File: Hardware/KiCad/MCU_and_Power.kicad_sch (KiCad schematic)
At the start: 67 parts

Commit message: Final schematic changes made, added some annotations
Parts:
- HSE?: footprint (none) -> Crystal:Crystal_SMD_3225-4Pin_3.2x2.5mm
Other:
- note added: "ADC1_INP3"
- note added: "Pins with possible external connections have current limiting resistors"
- note added: "TIM3_CH4"
- note added: "TIM4_CH1"
- note added: "TIM4_CH2"
- note added: "TIM4_CH3"
- note added: "TIM4_CH4"
- note added: "TIM5_CH3"
- note added: "TIM5_CH4"
- note removed: "Pins with external connection have current limiting resistors"
- note removed: "check"

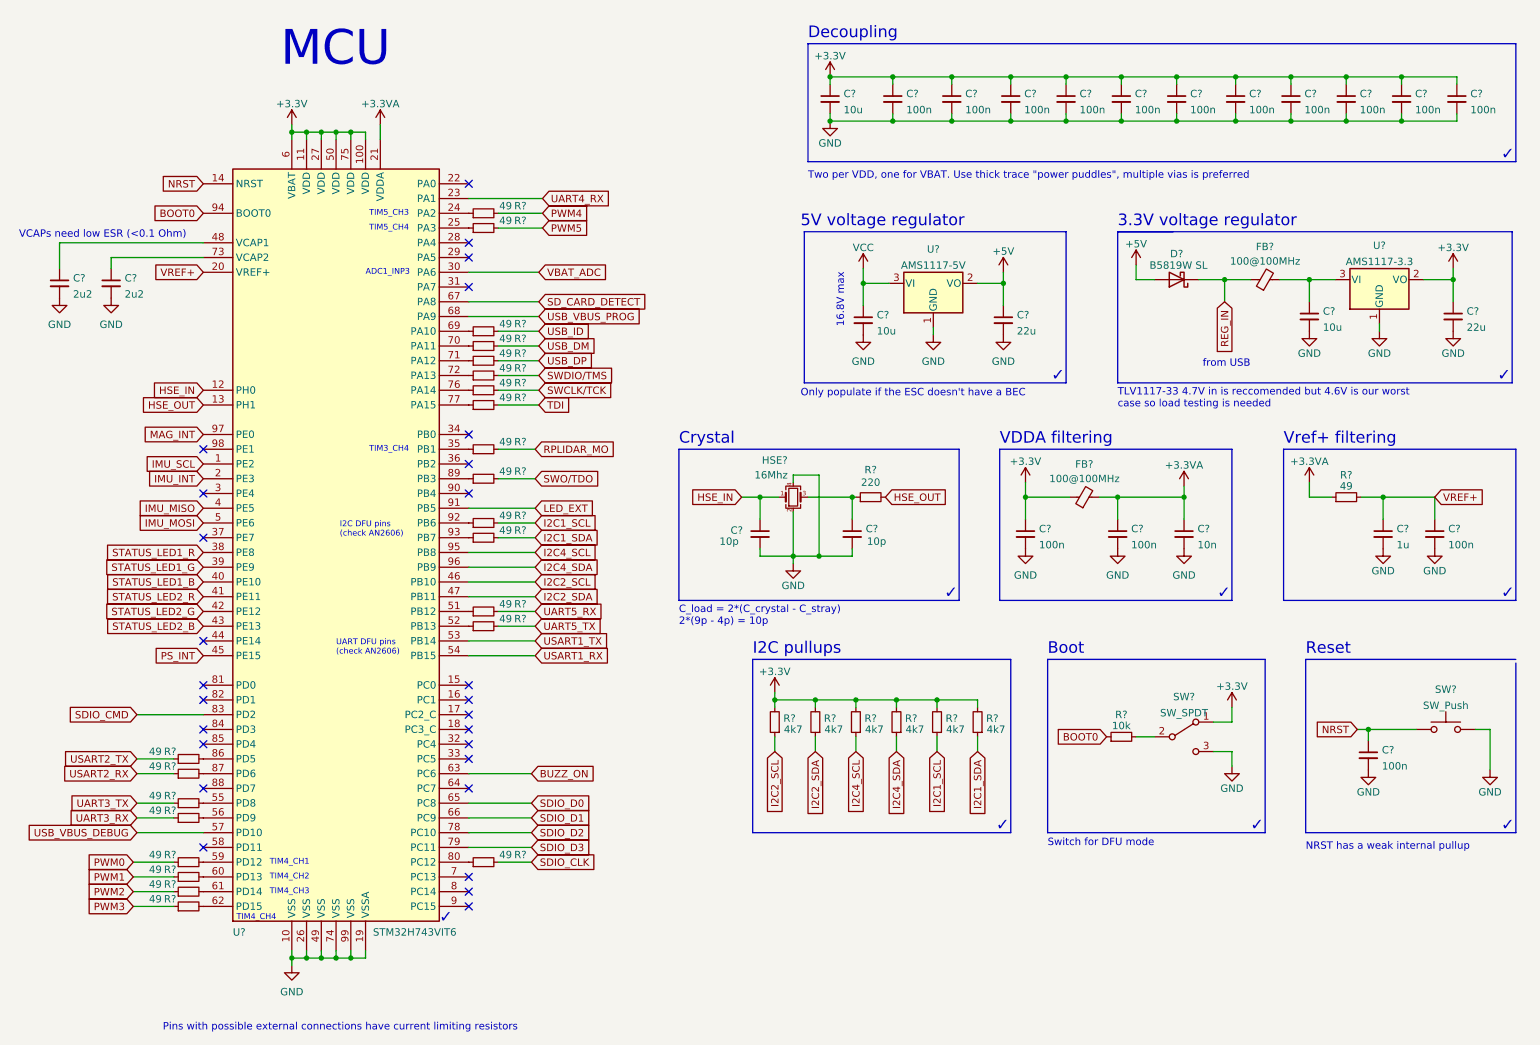
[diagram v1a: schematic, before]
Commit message: Fixed ERC errors
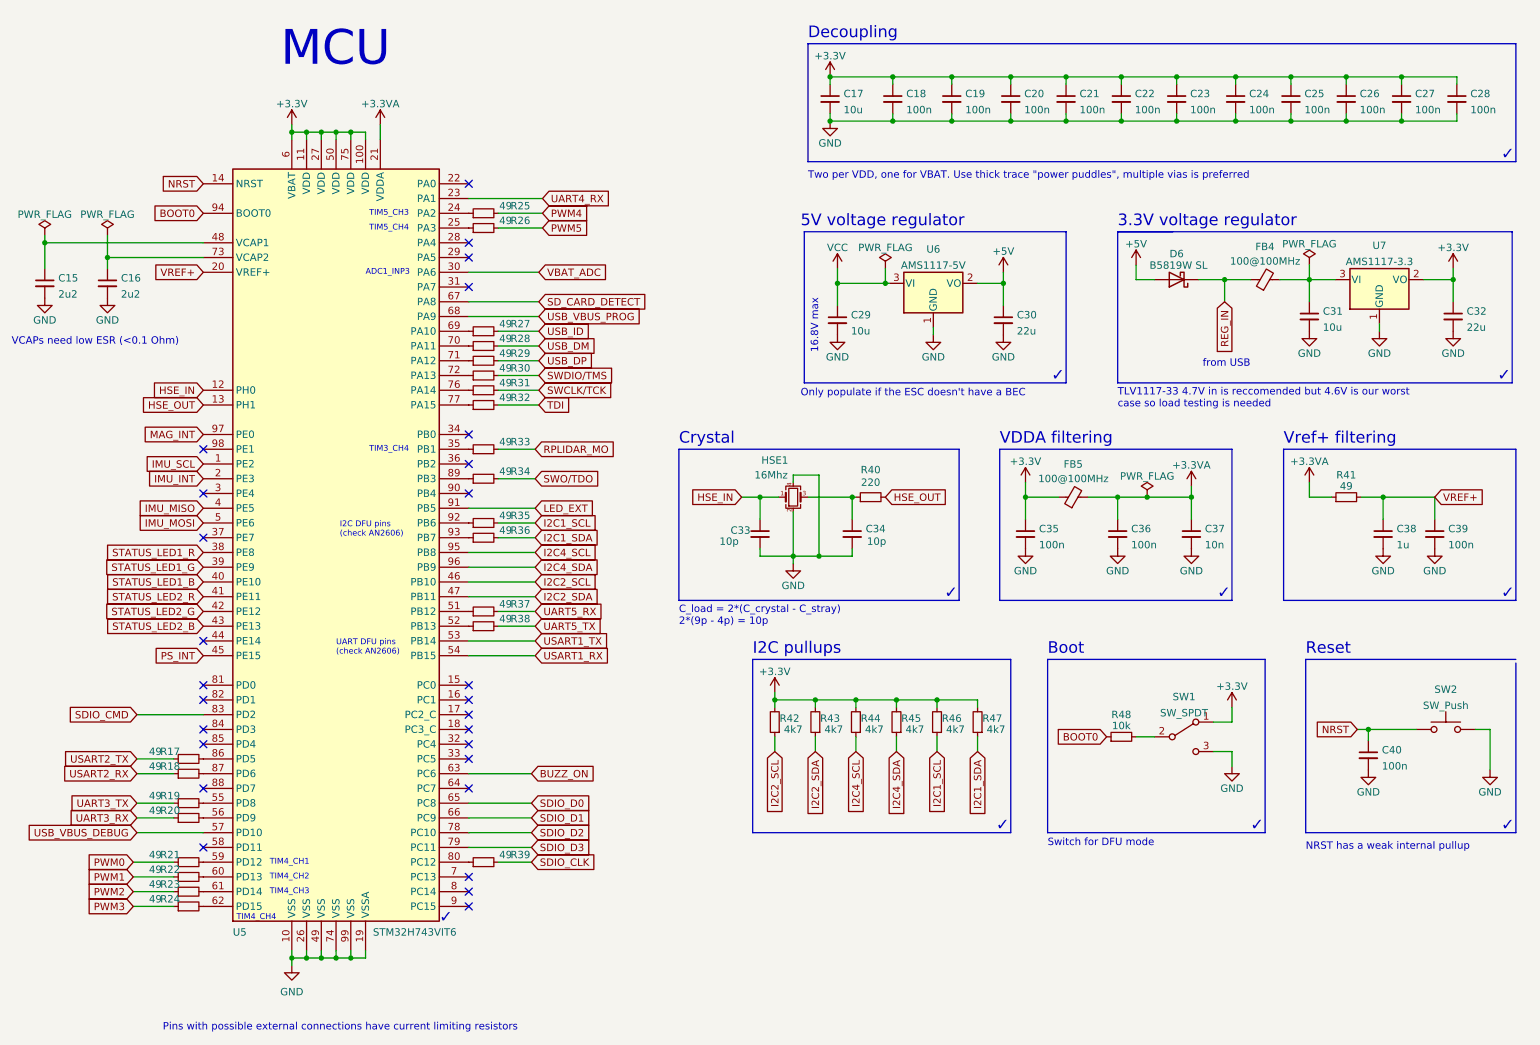
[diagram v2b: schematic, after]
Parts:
- gave numbers to parts that had none: 67
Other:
- moved on the sheet: C15, C16, C29, C37, FB5

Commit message: Made a general PCB layout
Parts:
- removed R27, R30, R31, R32, R34: 49, Resistor_SMD:R_0402_1005Metric, symbol Device:R_Small
- added C53: 100n, Capacitor_SMD:C_0402_1005Metric, symbol Device:C_Small
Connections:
- net +3V3: now also C53.1
- net GND: now also C53.2
- net SWCLK/TCK: now also U5.76 (PA14)
- net SWDIO/TMS: now also U5.72 (PA13)
- net SWO/TDO: now also U5.89 (PB3)
- net TDI: now also U5.77 (PA15)
- net USB_ID: now also U5.69 (PA10)
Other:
- moved on the sheet: C17

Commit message: Almost finished all routing
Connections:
- net BUZZ_ON: now also U5.31 (PA7); no longer U5.63 (PC6)
- net LED_EXT: now also U5.98 (PE1); no longer U5.91 (PB5)
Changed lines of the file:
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@@
   (junction (at 205.74 100.33) (diameter 0) (color 0 0 0 0)
   )
+  (no_connect (at 93.98 147.955))
+  (no_connect (at 93.98 102.235))
   (no_connect (at 93.98 46.355))
   (no_connect (at 93.98 150.495))
@@
   (no_connect (at 48.26 140.335))
   (no_connect (at 93.98 56.515))
-  (no_connect (at 93.98 64.135))
   (no_connect (at 93.98 89.535))
   (no_connect (at 93.98 59.055))
@@
   (no_connect (at 93.98 142.875))
   (no_connect (at 48.26 99.695))
-  (no_connect (at 48.26 92.075))
   (no_connect (at 48.26 107.315))
   (wire (pts (xy 68.58 37.465) (xy 71.12 37.465))
@@
     (stroke (width 0) (type default) (color 0 0 0 0))
   )
-  (wire (pts (xy 93.98 102.235) (xy 105.41 102.235))
-    (stroke (width 0) (type default) (color 0 0 0 0))
-  )
   (wire (pts (xy 20.955 56.515) (xy 20.955 60.96))
     (stroke (width 0) (type default) (color 0 0 0 0))
@@
   )
   (wire (pts (xy 238.76 100.33) (xy 242.57 100.33))
-    (stroke (width 0) (type default) (color 0 0 0 0))
-  )
-  (wire (pts (xy 104.775 147.955) (xy 93.98 147.955))
     (stroke (width 0) (type default) (color 0 0 0 0))
   )
@@
   )
   (wire (pts (xy 105.41 127.635) (xy 93.98 127.635))
+    (stroke (width 0) (type default) (color 0 0 0 0))
+  )
+  (wire (pts (xy 106.045 64.135) (xy 93.98 64.135))
     (stroke (width 0) (type default) (color 0 0 0 0))
   )
@@
     )
   )
+  (global_label "BUZZ_ON" (shape input) (at 106.045 64.135 0) (fields_autoplaced)
+    (effects (font (size 1.27 1.27)) (justify left))
+    (property "Intersheet References" "${INTERSHEET_REFS}" (id 0) (at 117.1062 64.2144 0)
+      (effects (font (size 1.27 1.27)) (justify left) hide)
+    )
+  )
   (global_label "SDIO_CLK" (shape input) (at 104.775 163.195 0) (fields_autoplaced)
     (effects (font (size 1.27 1.27)) (justify left))
@@
     )
   )
-  (global_label "BUZZ_ON" (shape input) (at 104.775 147.955 0) (fields_autoplaced)
-    (effects (font (size 1.27 1.27)) (justify left))
-    (property "Intersheet References" "${INTERSHEET_REFS}" (id 0) (at 115.8362 148.0344 0)
-      (effects (font (size 1.27 1.27)) (justify left) hide)
-    )
-  )
   (global_label "USB_VBUS_DEBUG" (shape input) (at 36.83 158.115 180) (fields_autoplaced)
     (effects (font (size 1.27 1.27)) (justify right))
@@
     )
   )
-  (global_label "LED_EXT" (shape input) (at 105.41 102.235 0) (fields_autoplaced)
-    (effects (font (size 1.27 1.27)) (justify left))
-    (property "Intersheet References" "${INTERSHEET_REFS}" (id 0) (at 115.5641 102.3144 0)
-      (effects (font (size 1.27 1.27)) (justify left) hide)
-    )
-  )
   (global_label "VREF+" (shape input) (at 260.35 100.33 0) (fields_autoplaced)
     (effects (font (size 1.27 1.27)) (justify left))
@@
     )
   )
+  (global_label "LED_EXT" (shape input) (at 48.26 92.075 180) (fields_autoplaced)
+    (effects (font (size 1.27 1.27)) (justify right))
+    (property "Intersheet References" "${INTERSHEET_REFS}" (id 0) (at 38.1059 91.9956 0)
+      (effects (font (size 1.27 1.27)) (justify right) hide)
+    )
+  )

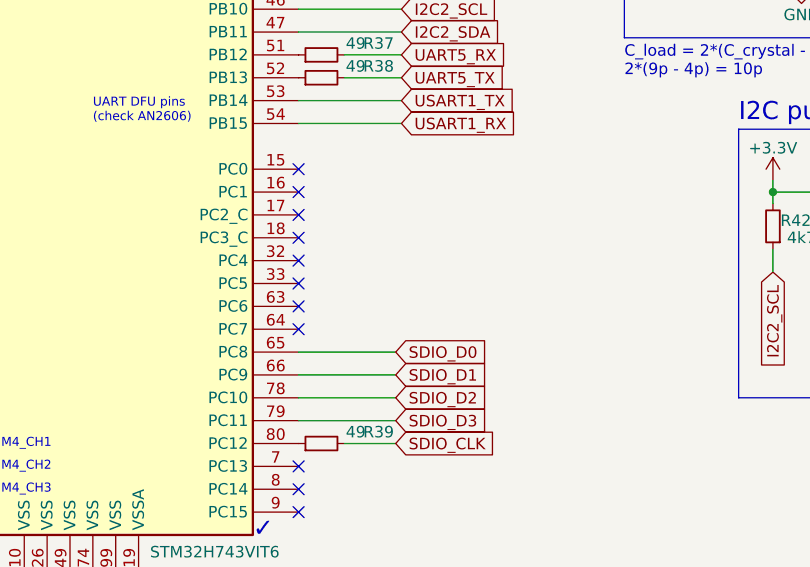
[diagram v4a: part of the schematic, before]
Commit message: Added a 5V sense line
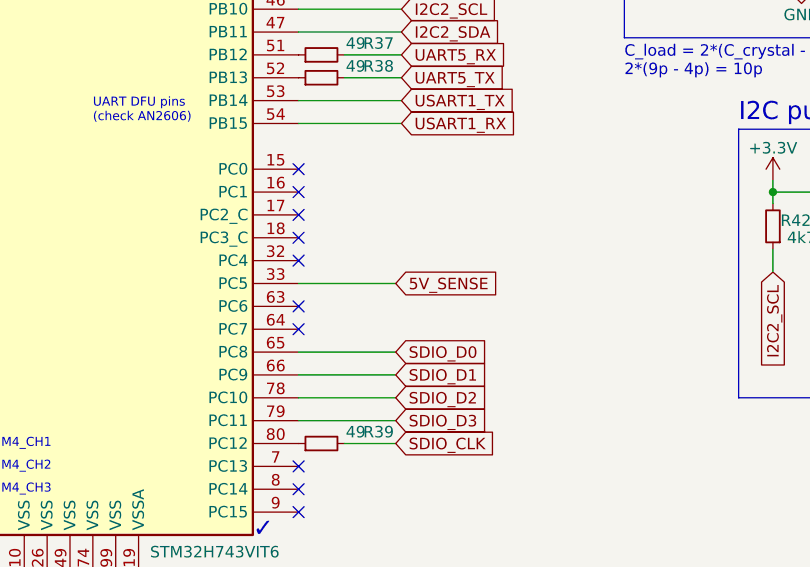
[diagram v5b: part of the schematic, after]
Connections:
- net 5V_SENSE: now reaches U5.33 (PC5)
- no-connect marks 27 -> 26
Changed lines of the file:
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@@
   (no_connect (at 93.98 165.735))
   (no_connect (at 93.98 170.815))
-  (no_connect (at 93.98 145.415))
   (no_connect (at 93.98 142.875))
   (no_connect (at 48.26 99.695))
@@
     (stroke (width 0) (type default) (color 0 0 0 0))
   )
+  (wire (pts (xy 93.98 145.415) (xy 104.775 145.415))
+    (stroke (width 0) (type default) (color 0 0 0 0))
+  )
   (wire (pts (xy 68.58 178.435) (xy 68.58 179.705))
     (stroke (width 0) (type default) (color 0 0 0 0))
@@
     )
   )
+  (global_label "5V_SENSE" (shape input) (at 104.775 145.415 0) (fields_autoplaced)
+    (effects (font (size 1.27 1.27)) (justify left))
+    (property "Intersheet References" "${INTERSHEET_REFS}" (id 0) (at 116.5014 145.3356 0)
+      (effects (font (size 1.27 1.27)) (justify left) hide)
+    )
+  )

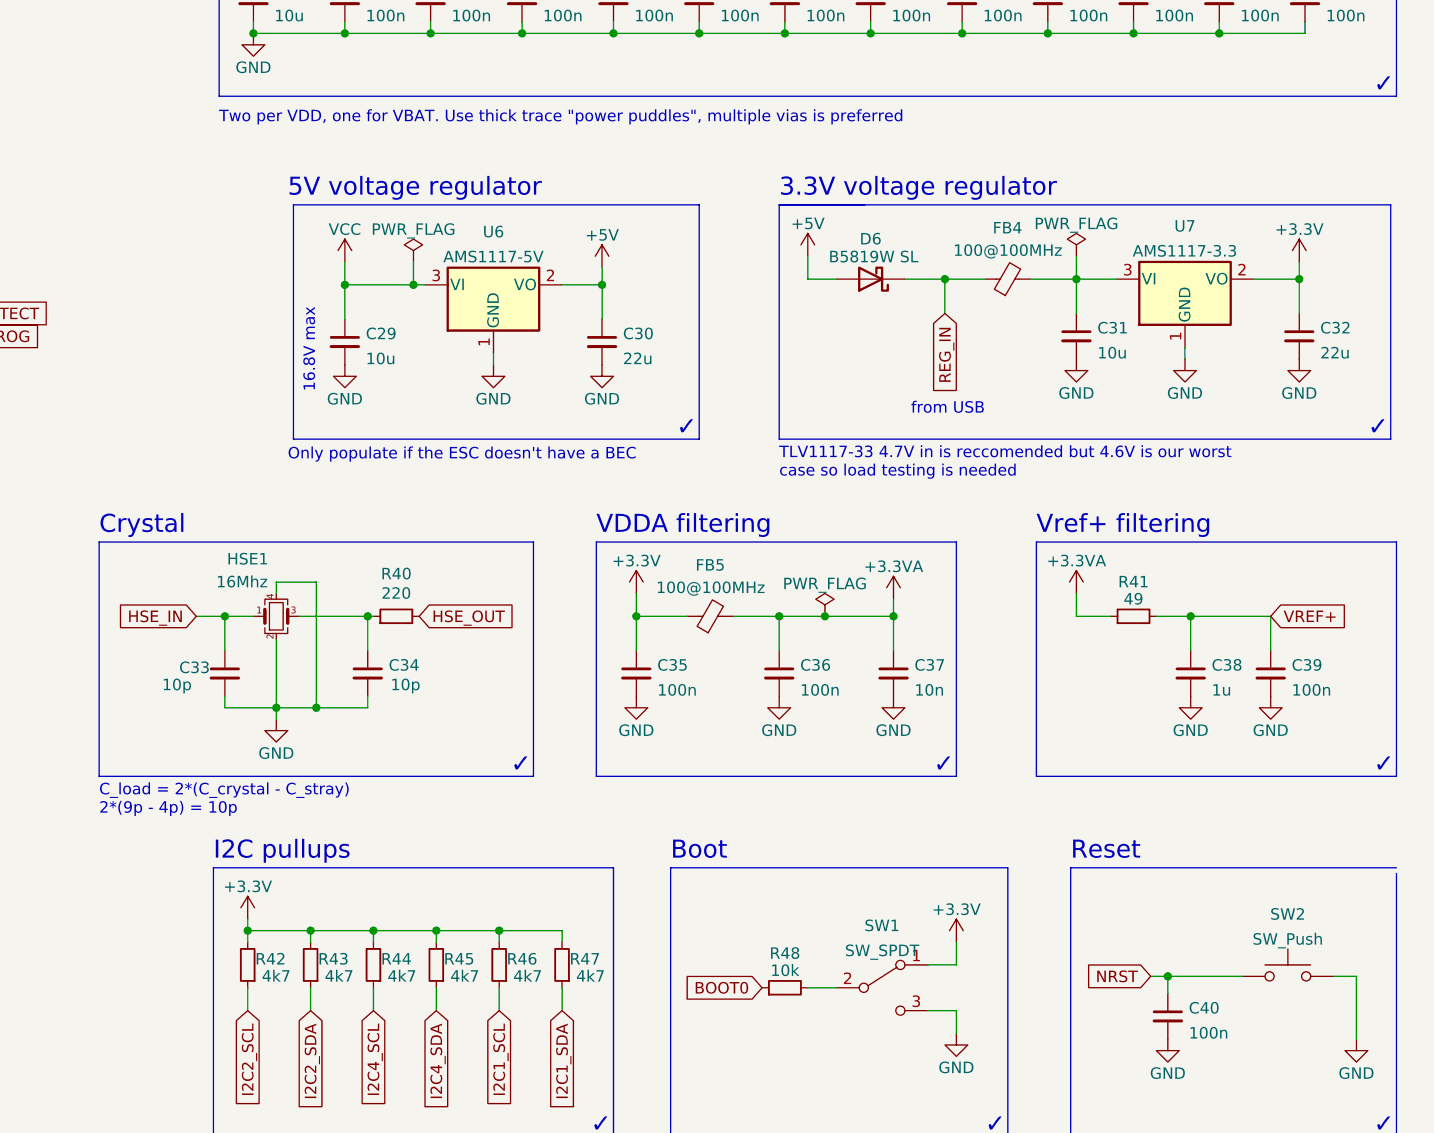
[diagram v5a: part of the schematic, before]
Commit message: Changed the 3.3V LDO to one that supports a lower Vin so sub 5V USB supplies are less likely to pose a problem
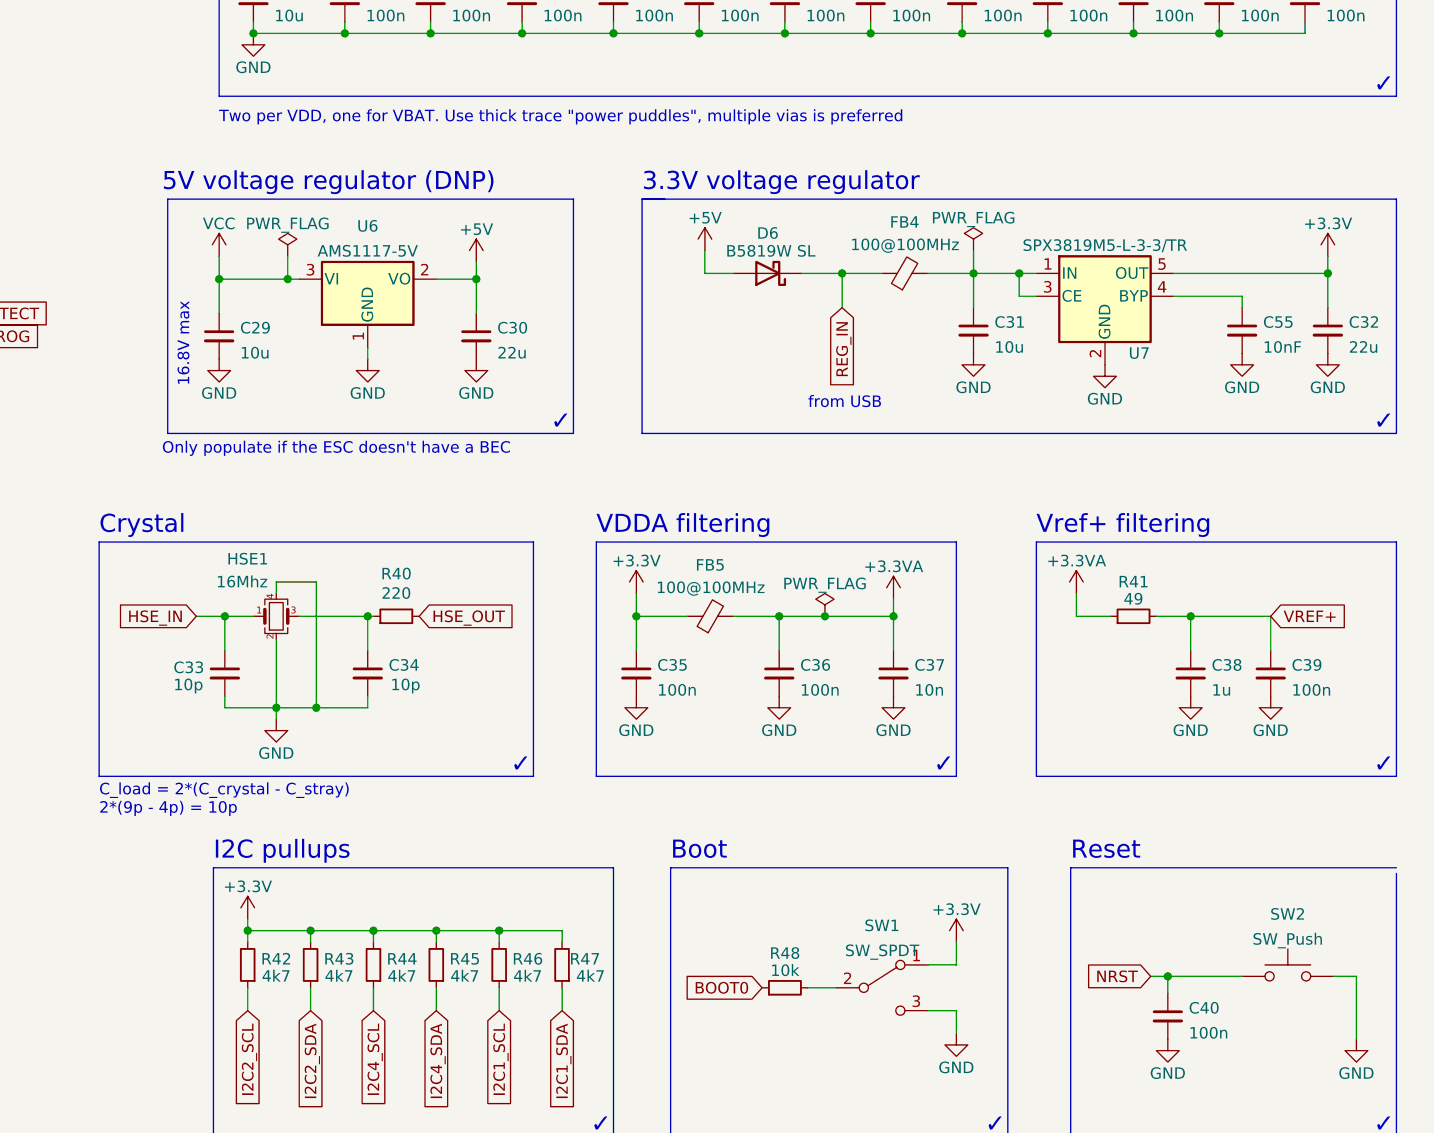
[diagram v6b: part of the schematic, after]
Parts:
- removed U7: AMS1117-3.3, Package_TO_SOT_SMD:SOT-223-3_TabPin2, symbol Regulator_Linear:AMS1117-3.3
- added C55: 10nF, Capacitor_SMD:C_0402_1005Metric, symbol Device:C_Small
- added U7: SPX3819M5-L-3-3/TR, Package_TO_SOT_SMD:SOT-23-5, symbol flightController:SPX3819M5-L-3-3/TR
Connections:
- net +3V3: now also U7.5 (OUT)
- net GND: now also C55.2, U7.2 (GND)
- net at C31.1, FB4.2: now also U7.1 (IN), U7.3 (CE)
- new net: C55.1, U7.4 (BYP)
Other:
- note added: "5V voltage regulator (DNP)"
- note removed: "5V voltage regulator"
- note removed: "TLV1117-33 4.7V in is reccomended but 4.6V is our worst case so load testing is needed"
- moved on the sheet: C29, C30, C31, C32, D6, FB4, U6
